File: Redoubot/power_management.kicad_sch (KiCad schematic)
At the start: 28 parts, among them U4 BQ25896RTWR, U5 BQ27220YZFR

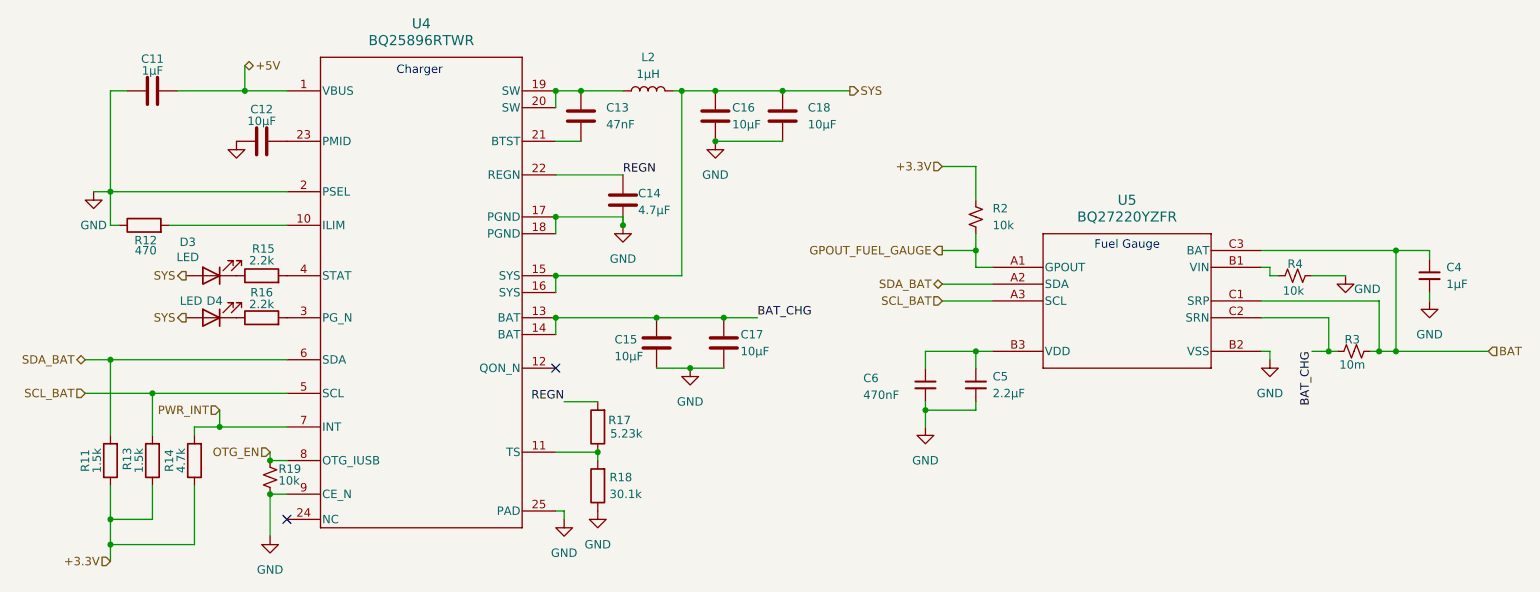
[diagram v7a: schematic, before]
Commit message: replaced the footprints for resistors with 0402 variants
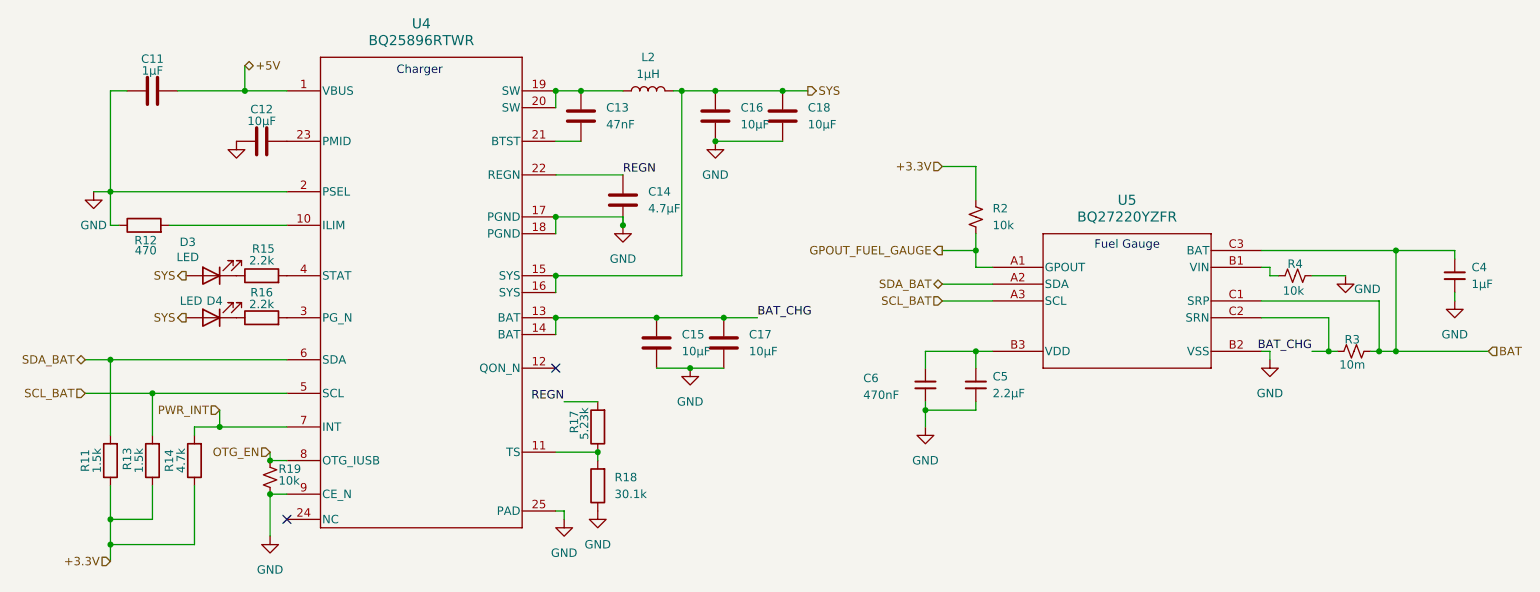
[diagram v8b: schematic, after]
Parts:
- R11, R12, R13, R14, R15, R16, R17, R18, R2, R4: footprint Resistor_SMD:R_0603_1608Metric -> Resistor_SMD:R_0402_1005Metric
- R19: footprint (none) -> Resistor_SMD:R_0402_1005Metric
- R3: footprint Resistor_SMD:R_0805_2012Metric -> Resistor_SMD:R_0402_1005Metric
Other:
- moved on the sheet: C4
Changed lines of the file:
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@@
 	)
 	(junction
-		(at 162.56 71.12)
+		(at 123.19 39.37)
 		(diameter 0)
 		(color 0 0 0 0)
 	)
 	(junction
-		(at 226.06 71.12)
+		(at 162.56 71.12)
 		(diameter 0)
 		(color 0 0 0 0)
 	)
 	(junction
-		(at 102.87 31.75)
+		(at 226.06 71.12)
 		(diameter 0)
 		(color 0 0 0 0)
 	)
 	(junction
-		(at 99.06 31.75)
+		(at 102.87 31.75)
 		(diameter 0)
 		(color 0 0 0 0)
 	)
 	(junction
-		(at 123.19 39.37)
+		(at 99.06 31.75)
 		(diameter 0)
 		(color 0 0 0 0)
@@
 	(wire
 		(pts
-			(xy 133.35 31.75) (xy 143.51 31.75)
+			(xy 133.35 31.75) (xy 137.16 31.75)
 		)
 		(stroke
@@
 	(wire
 		(pts
+			(xy 123.19 39.37) (xy 133.35 39.37)
+		)
+		(stroke
+			(width 0)
+			(type default)
+		)
+	)
+	(wire
+		(pts
 			(xy 44.45 82.55) (xy 58.42 82.55)
 		)
@@
 	(wire
 		(pts
-			(xy 205.74 55.88) (xy 231.14 55.88)
+			(xy 205.74 55.88) (xy 234.95 55.88)
 		)
 		(stroke
@@
 	(wire
 		(pts
-			(xy 123.19 39.37) (xy 133.35 39.37)
-		)
-		(stroke
-			(width 0)
-			(type default)
-		)
-	)
-	(wire
-		(pts
 			(xy 27.94 72.39) (xy 31.75 72.39)
 		)
@@
 	(wire
 		(pts
-			(xy 231.14 63.5) (xy 231.14 62.23)
+			(xy 234.95 63.5) (xy 234.95 62.23)
 		)
 		(stroke
@@
 	(wire
 		(pts
-			(xy 231.14 55.88) (xy 231.14 57.15)
+			(xy 234.95 55.88) (xy 234.95 57.15)
 		)
 		(stroke
@@
 	)
 	(label "BAT_CHG"
-		(at 213.36 71.12 270)
+		(at 213.36 71.12 180)
 		(effects
 			(font
@@
 	(hierarchical_label "SYS"
 		(shape output)
-		(at 143.51 31.75 0)
+		(at 137.16 31.75 0)
 		(effects
 			(font
@@
 	(symbol
 		(lib_id "Device:C_Small")
-		(at 231.14 59.69 0)
+		(at 234.95 59.69 0)
 		(unit 1)
 		(body_style 1)
@@
 		(fields_autoplaced yes)
 		(property "Reference" "C4"
-			(at 233.68 58.4199 0)
+			(at 237.49 58.4199 0)
 			(show_name no)
 			(do_not_autoplace no)
@@
 		)
 		(property "Value" "1µF"
-			(at 233.68 60.9599 0)
+			(at 237.49 60.9599 0)
 			(show_name no)
 			(do_not_autoplace no)
@@
 		)
 		(property "Footprint" "Capacitor_SMD:C_0402_1005Metric"
-			(at 231.14 59.69 0)
+			(at 234.95 59.69 0)
 			(hide yes)
 			(show_name no)
@@
 		)
 		(property "Datasheet" ""
-			(at 231.14 59.69 0)
+			(at 234.95 59.69 0)
 			(hide yes)
 			(show_name no)
@@
 		)
 		(property "Description" "Unpolarized capacitor, small symbol"
-			(at 231.14 69.85 0)
+			(at 234.95 69.85 0)
 			(hide yes)
 			(show_name no)
@@
 		(in_pos_files yes)
 		(dnp no)
+		(fields_autoplaced yes)
 		(property "Reference" "C17"
-			(at 127 68.58 0)
+			(at 128.27 68.5799 0)
 			(show_name no)
 			(do_not_autoplace no)
@@
 		)
 		(property "Value" "10µF"
-			(at 127 71.12 0)
+			(at 128.27 71.1199 0)
 			(show_name no)
 			(do_not_autoplace no)
@@
 	(symbol
 		(lib_id "power:GND")
-		(at 231.14 63.5 0)
+		(at 234.95 63.5 0)
 		(unit 1)
 		(body_style 1)
@@
 		(fields_autoplaced yes)
 		(property "Reference" "#PWR06"
-			(at 231.14 69.85 0)
+			(at 234.95 69.85 0)
 			(hide yes)
 			(show_name no)
@@
 		)
 		(property "Value" "GND"
-			(at 231.14 68.58 0)
+			(at 234.95 68.58 0)
 			(show_name no)
 			(do_not_autoplace no)
@@
 		)
 		(property "Footprint" ""
-			(at 231.14 63.5 0)
+			(at 234.95 63.5 0)
 			(hide yes)
 			(show_name no)
@@
 		)
 		(property "Datasheet" ""
-			(at 231.14 63.5 0)
+			(at 234.95 63.5 0)
 			(hide yes)
 			(show_name no)
@@
 		)
 		(property "Description" "Power symbol creates a global label with name \"GND\" , ground"
-			(at 231.14 63.5 0)
+			(at 234.95 63.5 0)
 			(hide yes)
 			(show_name no)
@@
 			)
 		)
-		(property "Footprint" "Resistor_SMD:R_0603_1608Metric"
+		(property "Footprint" "Resistor_SMD:R_0402_1005Metric"
 			(at 54.61 67.818 90)
 			(hide yes)
@@
 			)
 		)
-		(property "Footprint" "Resistor_SMD:R_0603_1608Metric"
+		(property "Footprint" "Resistor_SMD:R_0402_1005Metric"
 			(at 39.878 87.63 90)
 			(hide yes)
@@
 			)
 		)
-		(property "Footprint" "Resistor_SMD:R_0603_1608Metric"
+		(property "Footprint" "Resistor_SMD:R_0402_1005Metric"
 			(at 210.82 59.69 0)
 			(hide yes)
@@
 			)
 		)
-		(property "Footprint" "Resistor_SMD:R_0603_1608Metric"
+		(property "Footprint" "Resistor_SMD:R_0402_1005Metric"
 			(at 162.56 50.8 0)
 			(hide yes)
@@
 			)
 		)
-		(property "Footprint" "Resistor_SMD:R_0603_1608Metric"
+		(property "Footprint" "Resistor_SMD:R_0402_1005Metric"
 			(at 46.228 87.63 90)
 			(hide yes)
@@
 		(in_pos_files yes)
 		(dnp no)
+		(fields_autoplaced yes)
 		(property "Reference" "C15"
-			(at 107.95 69.342 0)
+			(at 118.11 68.5799 0)
 			(show_name no)
 			(do_not_autoplace no)
@@
 		)
 		(property "Value" "10µF"
-			(at 107.95 71.882 0)
+			(at 118.11 71.1199 0)
 			(show_name no)
 			(do_not_autoplace no)
@@
 			)
 		)
-		(property "Footprint" ""
+		(property "Footprint" "Resistor_SMD:R_0402_1005Metric"
 			(at 55.88 90.17 0)
 			(hide yes)
@@
 			)
 		)
-		(property "Footprint" "Resistor_SMD:R_0805_2012Metric"
+		(property "Footprint" "Resistor_SMD:R_0402_1005Metric"
 			(at 219.71 71.12 0)
 			(hide yes)
@@
 			)
 		)
-		(property "Footprint" "Resistor_SMD:R_0603_1608Metric"
+		(property "Footprint" "Resistor_SMD:R_0402_1005Metric"
 			(at 36.83 53.848 90)
 			(hide yes)
@@
 		(dnp no)
 		(property "Reference" "R17"
-			(at 108.712 81.534 0)
+			(at 101.854 81.788 90)
 			(show_name no)
 			(do_not_autoplace no)
@@
 		)
 		(property "Value" "5.23k"
-			(at 109.728 83.566 0)
+			(at 103.378 82.042 90)
 			(show_name no)
 			(do_not_autoplace no)
@@
 			)
 		)
-		(property "Footprint" "Resistor_SMD:R_0603_1608Metric"
+		(property "Footprint" "Resistor_SMD:R_0402_1005Metric"
 			(at 107.188 82.55 90)
 			(hide yes)
@@
 		(in_pos_files yes)
 		(dnp no)
+		(fields_autoplaced yes)
 		(property "Reference" "C14"
-			(at 111.506 47.244 0)
+			(at 113.03 46.9899 0)
 			(show_name no)
 			(do_not_autoplace no)
@@
 		)
 		(property "Value" "4.7µF"
-			(at 111.506 49.784 0)
+			(at 113.03 49.5299 0)
 			(show_name no)
 			(do_not_autoplace no)
@@
 		(in_pos_files yes)
 		(dnp no)
+		(fields_autoplaced yes)
 		(property "Reference" "R18"
-			(at 107.188 90.17 0)
+			(at 107.95 90.1699 0)
 			(show_name no)
 			(do_not_autoplace no)
@@
 		)
 		(property "Value" "30.1k"
-			(at 107.188 92.71 0)
+			(at 107.95 92.7099 0)
 			(show_name no)
 			(do_not_autoplace no)
@@
 			)
 		)
-		(property "Footprint" "Resistor_SMD:R_0603_1608Metric"
+		(property "Footprint" "Resistor_SMD:R_0402_1005Metric"
 			(at 107.188 91.44 90)
 			(hide yes)
@@
 		(in_pos_files yes)
 		(dnp no)
+		(fields_autoplaced yes)
 		(property "Reference" "C16"
-			(at 125.73 34.2899 0)
+			(at 127 34.2899 0)
 			(show_name no)
 			(do_not_autoplace no)
@@
 		)
 		(property "Value" "10µF"
-			(at 125.73 36.8299 0)
+			(at 127 36.8299 0)
 			(show_name no)
 			(do_not_autoplace no)
@@
 			)
 		)
-		(property "Footprint" "Resistor_SMD:R_0603_1608Metric"
+		(property "Footprint" "Resistor_SMD:R_0402_1005Metric"
 			(at 33.528 87.63 90)
 			(hide yes)
@@
 			)
 		)
-		(property "Footprint" "Resistor_SMD:R_0603_1608Metric"
+		(property "Footprint" "Resistor_SMD:R_0402_1005Metric"
 			(at 54.61 61.468 90)
 			(hide yes)
